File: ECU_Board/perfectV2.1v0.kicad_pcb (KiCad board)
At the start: 4 copper layers, 100 x 100 mm, 172 parts, among them IC1 Trig Cond Socket, IC2 Trig Cond Socket, J1 Conn_02x20_Odd_Even, J2 Conn_01x02, J3 MAP_Connector, J4 Conn_01x06, J5 Conn_01x05, J6 Conn_01x05, J8 Conn_01x04, Q1 SSM3K318R, Q2 SSM3K318R, Q3 SSM3K318R, U1 Teensy4.1, U10 LM324A, U11 LM324A, U12 CD4504B, U13 CD4504B, U14 CD4504B, U2 LM2576-5G, U3 SP720, U4 BM2LC105, U5 BM2LC105, U6 TC4424A, U7 TC4424A, U8 BM2LC105, U9 BM2LC105

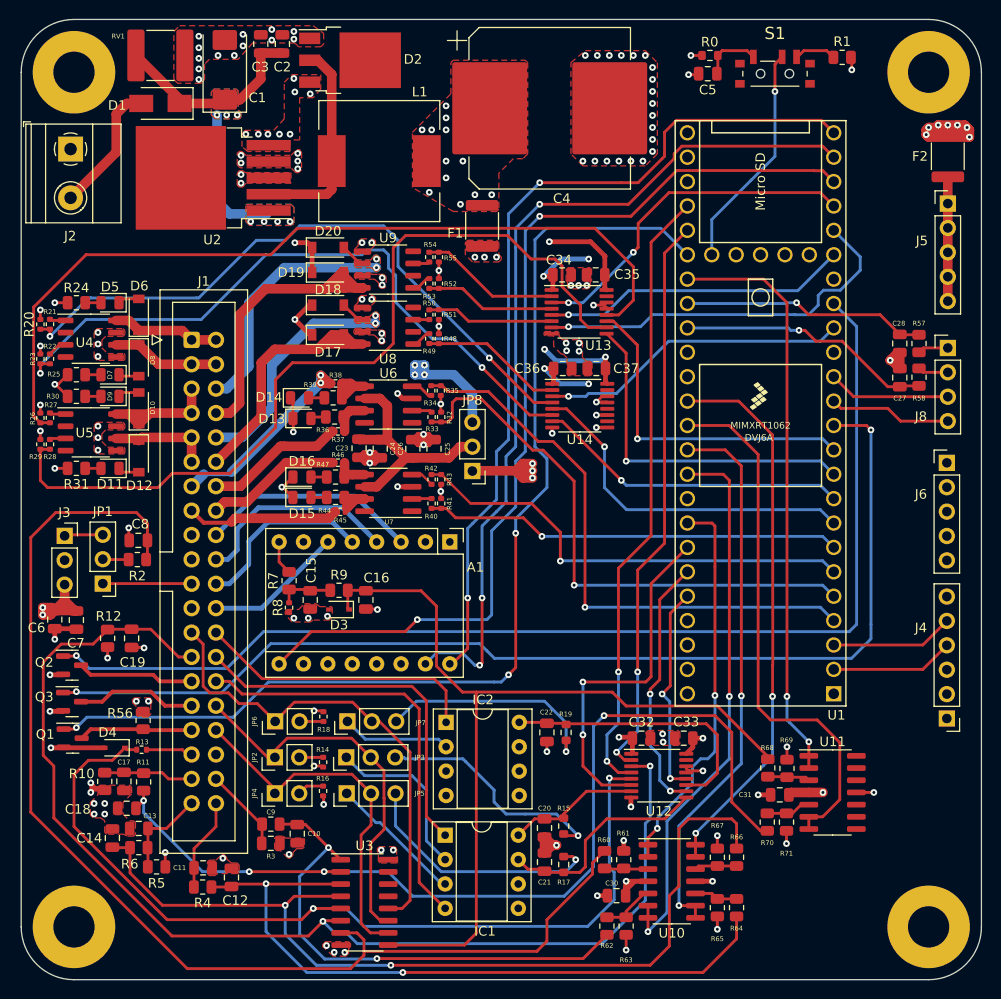
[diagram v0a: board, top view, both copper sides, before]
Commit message: Removed clutch input
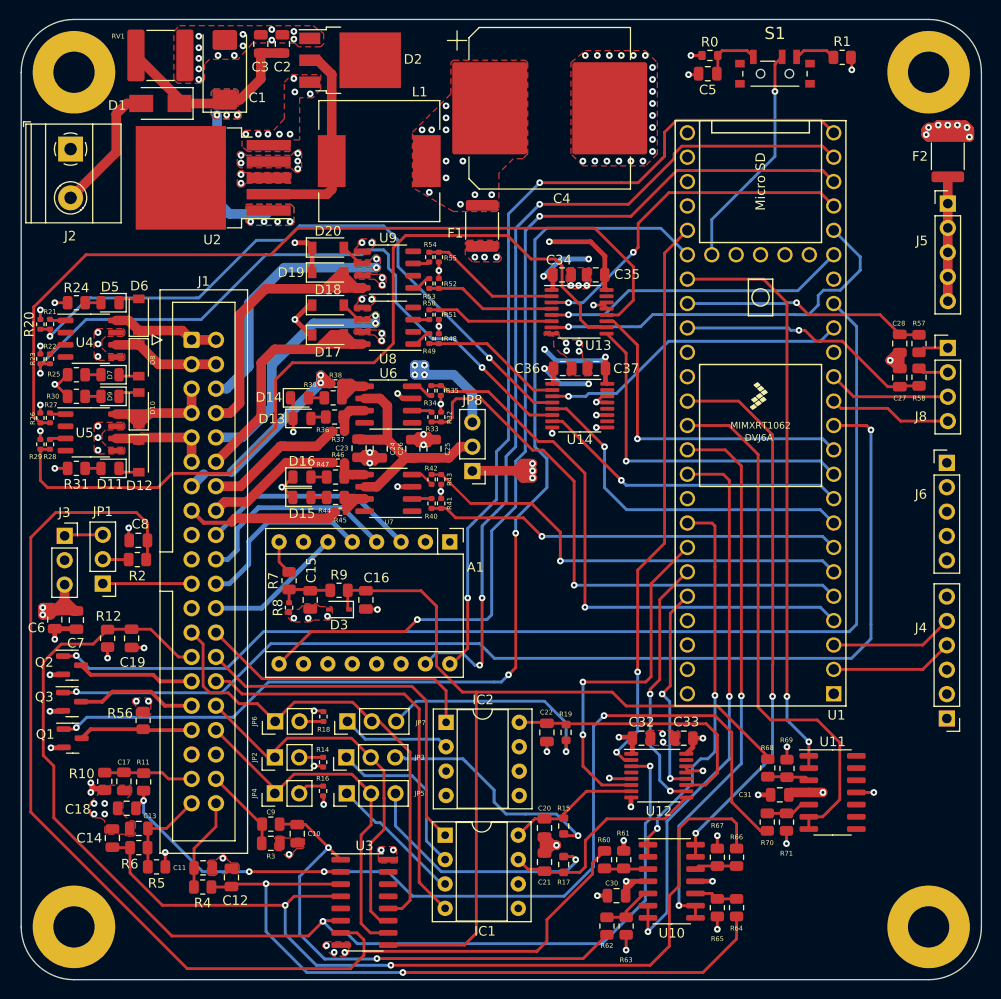
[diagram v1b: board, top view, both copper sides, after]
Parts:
- removed D4: PZU5.1B2A, Diode_SMD:D_SOD-323
- removed R13: 1kR, Resistor_SMD:R_0402_1005Metric
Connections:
- J1 pad 35: CLUTCH-IN -> VDDA
- U1 pad 28: MCU-CLUTCH -> unconnected-(U1-Pad28)
- U12 pad 4: MCU-CLUTCH -> unconnected-(U12-Pad4)
- U12 pad 5: CLUTCH-5V -> GND
- U3 pad 5: CLUTCH-5V -> unconnected-(U3-Pad5)
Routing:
- net CLUTCH-5V: track 93.9 -> 0.00 mm, vias 2 -> 0
- net MCU-CLUTCH: track 64.3 -> 0.00 mm, vias 2 -> 0
- net CLUTCH-IN: track 4.90 -> 0.00 mm
- net GND: track 92.9 -> 91.0 mm, vias 122 -> 123
